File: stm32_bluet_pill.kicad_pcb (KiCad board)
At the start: 4 copper layers, 45.8 x 19.6 mm, 80 parts, among them J1 Conn_01x15, J2 Conn_01x15, J3 BAT_SOCKET, J4 Conn_ARM_SWD_TagConnect_TC203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, J5 USB_C_Plug_USB2.0, Q1 DMG1012T, U1 STM32WB55RGVx, U3 AT25SL321-U, U4 BQ25185, U5 TPS62746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

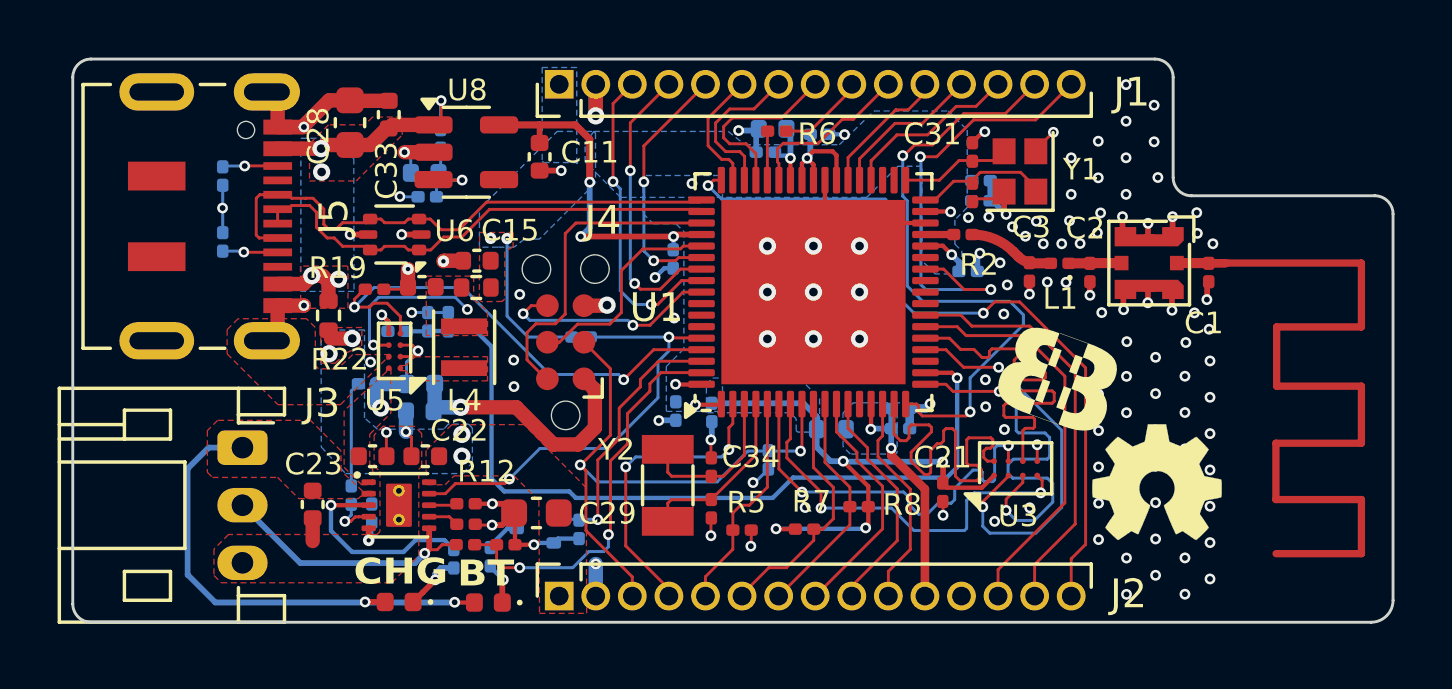
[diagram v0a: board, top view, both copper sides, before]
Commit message: Updated project
- Changed board stackup, trace-widths
- Changed VIA size
- Fixed fab drawings
- added CHG FLT LED
- Removed unnecessary files
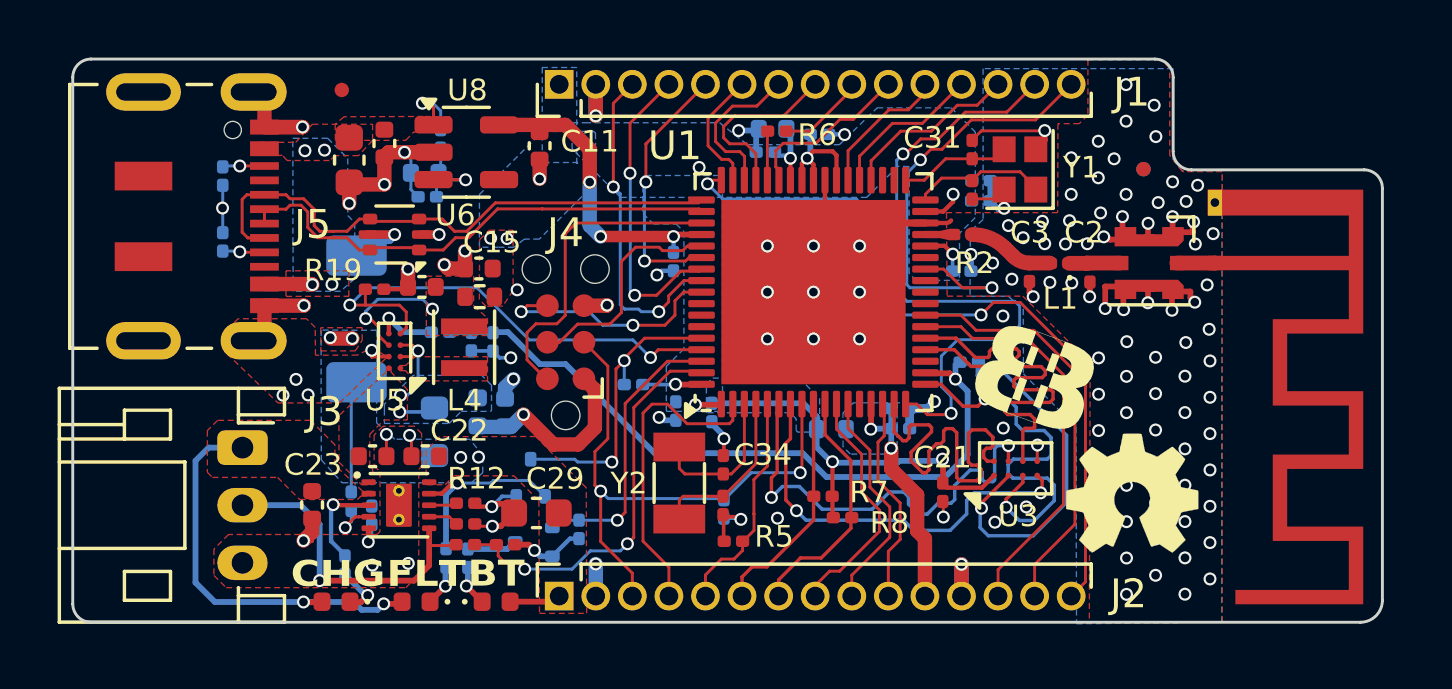
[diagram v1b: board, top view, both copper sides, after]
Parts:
- removed A1: 2.45GHz, user_antenna:nRF52_dongle_meander_F
- removed the REF** at (229.0, 143.7)
- added AE1: Antenna_Shield, RF_Antenna:Texas_SWRA117D_2.4GHz_Right, F.Cu at (231.1, 135.1)
- added D2: RB081LAM-20TR, Diode_SMD:D_SOD-128, B.Cu at (201.2, 137.0)
- added D5: LED, Diode_SMD:D_0402_1005Metric, F.Cu at (203.3, 146.9)
- added FID1: FID1, Fiducial:Fiducial_0.5mm_Mask1mm, F.Cu at (200.7, 129.1)
- added FID2: Fiducial, Fiducial:Fiducial_0.5mm_Mask1mm, F.Cu at (228.6, 131.8)
- added FID3: Fiducial, Fiducial:Fiducial_0.5mm_Mask1mm, B.Cu at (228.6, 131.8)
- added Q2: DMG1012T, Package_TO_SOT_SMD:SOT-523, B.Cu at (207.3, 142.6)
- added REF**: OSHW-Logo2_7.3x6mm_SilkScreen, Symbol:OSHW-Logo2_7.3x6mm_SilkScreen, F.Cu at (228.2, 143.8)
- C1: value 0.7PF -> 10NF; moved to B.Cu
- D3: value BAT54LP -> VSKY05301006-G4-08
- J4: value Conn_ARM_SWD_TagConnect_TC2030-NL -> J4
- R13: footprint Resistor_SMD:R_0201_0603Metric -> Resistor_SMD:R_0603_1608Metric
- R22: value 0R -> 420R; footprint Resistor_SMD:R_0402_1005Metric -> Resistor_SMD:R_0201_0603Metric; moved to B.Cu
- moved R22 9.36 mm to (204.3, 145.3)
- moved C1 8.88 mm to (222.5, 138.5), turned to 0 degrees
- moved R3 3.79 mm to (200.8, 145.6)
- moved C27 2.96 mm to (206.4, 140.3), turned to 90 degrees
- moved R13 2.86 mm to (203.9, 141.0), turned to -90 degrees
- moved R4 2.46 mm to (210.9, 139.3), turned to 180 degrees
- moved C10 2.30 mm to (214.0, 143.6)
- moved D3 2.20 mm to (205.4, 140.3), turned to -90 degrees
- moved D1 2.19 mm to (200.5, 146.9)
- moved C25 1.70 mm to (206.0, 137.8), turned to -90 degrees
- moved R17 1.66 mm to (205.2, 137.8), turned to -90 degrees
- moved R16 1.51 mm to (204.2, 137.5)
- moved R7 1.31 mm to (217.4, 143.2), turned to 180 degrees
- moved C28 1.30 mm to (201.0, 131.5), turned to -90 degrees
- moved C33 1.02 mm to (202.2, 130.9), turned to -90 degrees
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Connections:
- C1 pad 1: /BLE_MCU/BT_PCB_ANT -> VIN_SNS_ADC1_IN9
- D4 pad 2: PPVAR_BAT -> PPVAR_VIN
- R22 pad 1: VBUS -> FLT_CHG_ODL
- R22 pad 2: PPVAR_VIN -> Net-(D5-K)
- R4 pad 2: FLT_CHG_L -> /BLE_MCU/FLT_CHG_OD
- U1 pad 64: FLT_CHG_L -> /BLE_MCU/FLT_CHG_OD
- U4 pad 9: FLT_CHG_L -> FLT_CHG_ODL
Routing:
- net GND: track 66.6 -> 89.3 mm, vias 133 -> 137
- net FLT_CHG_L: track 15.5 -> 0.00 mm, vias 2 -> 0
- net /BLE_MCU/FLT_CHG_OD: track 0.00 -> 10.4 mm, vias 0 -> 2
- net PP1800_ALW: track 35.5 -> 27.4 mm, vias 12 -> 10
- net FLT_CHG_ODL: track 0.00 -> 6.89 mm, vias 0 -> 1
- net /POWER/CHG_LED_GRN: track 7.08 -> 3.14 mm
- net VIN_SNS_ADC1_IN9: track 28.9 -> 25.1 mm
- net VBUS: track 11.0 -> 7.59 mm
- net PPVAR_BAT: track 17.0 -> 14.4 mm
- net PP3300_DBG: track 9.25 -> 6.78 mm
- net /POWER/CHGR_BAT_THERM: track 9.31 -> 11.2 mm
- net PPVAR_VIN: track 4.39 -> 6.22 mm
- net /BLE_MCU/QSPI_MEM_D1: track 13.9 -> 15.7 mm
- net PP3300_VDDUSB: track 12.4 -> 10.9 mm
- net Net-(D5-K): track 0.00 -> 1.43 mm, vias 0 -> 1
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- added copper zone on B.Cu, net GND
- added copper zone on B.Cu, net PPVAR_SYS
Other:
- board size 45.8 x 19.6 mm -> 45.5 x 19.6 mm
- board text added: "0"
- board text added: "0 mm"
- board text added: "0.01 mm"
- board text added: "0.0152 mm"
- board text added: "0.02"
- board text added: "0.035 mm"
- board text added: "0.0764 mm"
- board text added: "0.1020 mm / 0.1000 mm"
- board text added: "0.2000 mm"
- board text added: "0.865 mm"
- board text added: "1"
- board text added: "1.1382 mm"
- board text added: "1080"
- board text added: "3.3"
- board text added: "3.91"
- board text added: "4"
- board text added: "4.6"
- board text added: "45.4770 mm x 19.5580 mm"
- board text added: "B.Cu"
- board text added: "B.Mask"
- board text added: "B.Paste"
- board text added: "B.Silkscreen"
- board text added: "BOARD CHARACTERISTICS"
- board text added: "Blue"
- board text added: "Board Thickness:"
- board text added: "Board overall dimensions:"
- board text added: "Bottom Silk Screen"
- board text added: "Bottom Solder Mask"
- board text added: "Bottom Solder Paste"
- board text added: "Castellated pads:"
- board text added: "Color"
- board text added: "Copper Finish:"
- board text added: "Copper Layer Count:"
- board text added: "Dielectric 1"
- board text added: "Dielectric 2"
- board text added: "Dielectric 3"
- board text added: "Edge card connectors:"
- board text added: "Epsilon R"
- board text added: "F.Cu"
- board text added: "F.Mask"
- board text added: "F.Paste"
- board text added: "F.Silkscreen"
- board text added: "FLT"
- board text added: "FR4"
- board text added: "FR4 natural"
- board text added: "IMPEDANCE TABLE"
- board text added: "Impedance Control:"
- board text added: "In1.Cu"
- board text added: "In2.Cu"
- board text added: "Layer Name"
- board text added: "Loss Tangent"
- board text added: "Material"
- board text added: "Min hole diameter:"
- board text added: "Min track/spacing:"
- board text added: "No"
- board text added: "No Copper Theiving in enclosed RF Areas"
- board text added: "None"
- board text added: "Not specified"
- board text added: "Plated Board Edge:"
- board text added: "Stackup (JLC04121H-1080)"
- board text added: "Thickness (mm)"
- board text added: "Top Silk Screen"
- board text added: "Top Solder Mask"
- board text added: "Top Solder Paste"
- board text added: "Type"
- board text added: "White"
- board text added: "Yes"
- board text added: "copper"
- board text added: "core"
- board text added: "prepreg"

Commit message: Various BOM and Bug Fixes * Changed Stackup to common JLCPCB stackup * Modified trace widths as per new stackup * Reduced drill hole size * Rotated uFL connector as per datasheet pinout * Added pop options for ADC voltage * removed some GPIO and added GND to headers * BOM changes for battery charger, USB connector etc. to support component specifications and USB standards. * Improved MCU bypass and power delivery routing * Various other small bug fixes
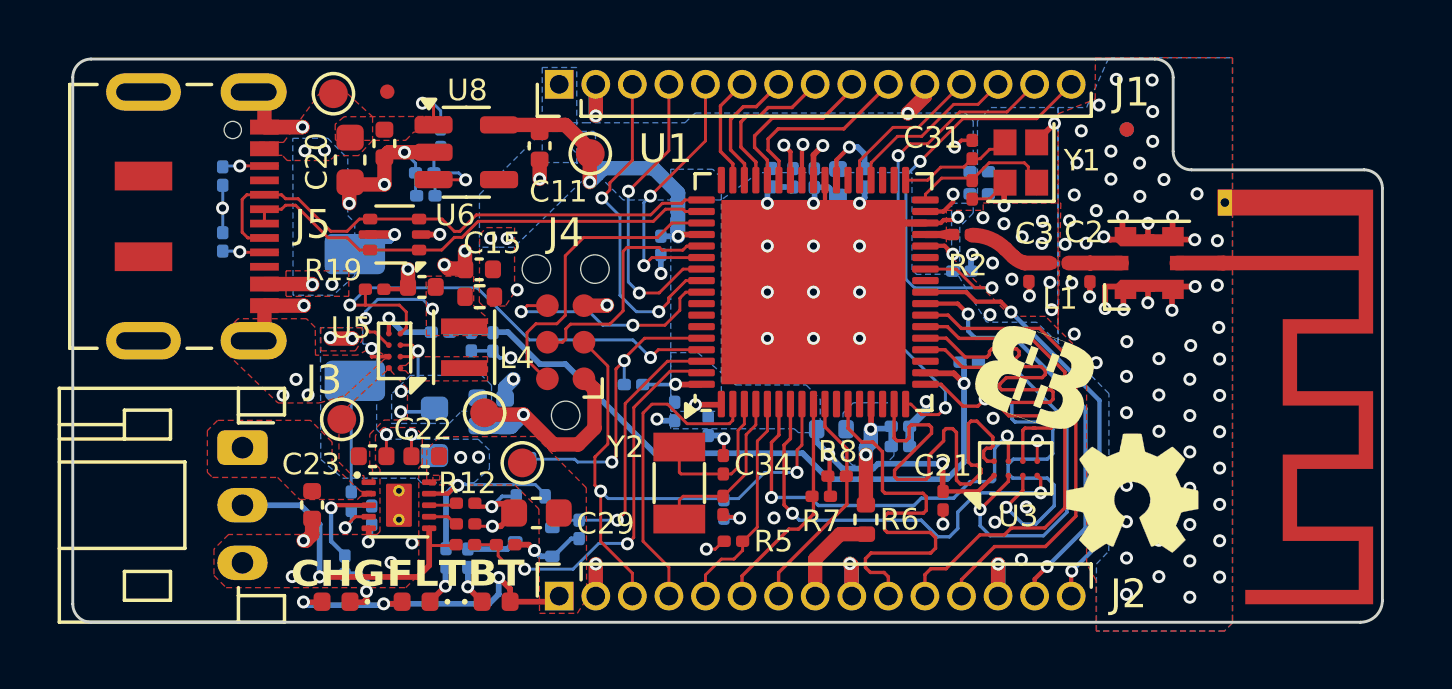
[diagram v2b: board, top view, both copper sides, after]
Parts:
- added C19: 100N, Capacitor_SMD:C_0201_0603Metric, B.Cu at (216.4, 132.1)
- added C20: 2.2U 35V, Capacitor_SMD:C_0603_1608Metric, F.Cu at (201.0, 131.5)
- added TP4: TestPoint, TestPoint:TestPoint_Pad_D1.0mm, F.Cu at (200.7, 140.5)
- added TP5: TestPoint, TestPoint:TestPoint_Pad_D1.0mm, F.Cu at (207.0, 142.0)
- added TP6: TestPoint, TestPoint:TestPoint_Pad_D1.0mm, F.Cu at (205.7, 140.3)
- added TP7: TestPoint, TestPoint:TestPoint_Pad_D1.0mm, F.Cu at (200.4, 129.2)
- added TP8: TestPoint, TestPoint:TestPoint_Pad_D1.0mm, F.Cu at (209.4, 131.3)
- AE1: value Antenna_Shield -> PCB MIFA
- C1: value 10NF -> 10N
- C10, C13, C17, C21, C25, C4, C5, C6, C7, C8, C9: value 100NF -> 100N
- C11, C12, C15: value 4.7UF -> 4.7U
- C14: value 100PF -> 100P
- C16: value 1UF -> 1.0U
- C2, C3: value 0.7PF -> 0.7P
- C22, C33: value 1.0UF -> 1.0U
- C23, C29: value 4.7UF -> 1.0U 35V
- C24: value 4.7UF -> 10U 10V
- C26: value 10UF -> 10U
- C27: value 1.0UF -> 1.0U 16V
- C28: value 4.7UF -> 100N; footprint Capacitor_SMD:C_0603_1608Metric -> Capacitor_SMD:C_0201_0603Metric; moved to B.Cu
- C30: footprint Capacitor_SMD:C_0402_1005Metric -> Capacitor_SMD:C_0201_0603Metric
- FID1: value FID1 -> Fiducial
- J3: value BAT_SOCKET -> PH_S3B-PH-K
- J4: value J4 -> Conn_ARM_SWD_TagConnect_TC2030-NL
- J5: value USB_C_Plug_USB2.0 -> DX07S016JA1R1500
- L1: value 2.2NH -> 2.2N
- L4: value 2.2UH -> 2.2U
- R22, R3: value 420R -> 470R
- R24: value 420R -> 1K
- R6: value 22R -> 0R; footprint Resistor_SMD:R_0201_0603Metric -> Resistor_SMD:R_0402_1005Metric
- Y1: value 32MHz -> ECS-320-8-37CKM
- Y2: value 32.768k -> SC32S-7PF20PPM
- moved C28 14.7 mm to (215.7, 132.1)
- moved R6 13.8 mm to (218.9, 144.0), turned to -90 degrees
- moved C6 3.56 mm to (218.9, 132.1), turned to -90 degrees
- moved C12 2.94 mm to (218.0, 132.3), turned to -90 degrees
- moved FID1 1.58 mm to (202.3, 129.2)
- moved C7 1.53 mm to (217.1, 132.2), turned to -90 degrees
- moved FID2 1.50 mm to (228.0, 130.5)
- moved FID3 1.50 mm to (228.0, 130.5)
- moved R8 1.45 mm to (217.9, 142.5)
- moved C9 0.71 mm to (211.8, 134.5)
- moved C16 0.62 mm to (220.1, 141.5)
- moved C17 0.62 mm to (220.1, 140.8)
- moved C4 0.50 mm to (213.5, 140.8)
- moved AE1 0.34 mm to (231.4, 135.1)
- moved C13 0.32 mm to (222.9, 131.9)
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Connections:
- C28 pad 1: VBUS -> PP1800_ALW
- D1 pad 2: PPVAR_BAT -> PPVAR_VIN
- D5 pad 2: PPVAR_BAT -> PPVAR_VIN
- J1 pad 11: GPIO_PE4 -> GND
- J2 pad 10: ADC1_IN5 -> STM_SAI1_SD_A
- J2 pad 11: PPVAR_ADC -> STM_SAI1_SCK_A
- J2 pad 12: GND -> STM_SAI1_FS_A
- J2 pad 13: STM_SAI1_SCK_A -> GND
- J2 pad 14: STM_SAI1_FS_A -> ADC1_IN13
- J2 pad 15: STM_SAI1_SD_A -> ADC1_IN14
- J2 pad 8: ADC1_IN3 -> Net-(J2-Pin_8)
- J2 pad 9: ADC1_IN4 -> GND
- R6 pad 1: Net-(U1-PB13) -> PPVAR_ADC
- R6 pad 2: SPI2_CLK_PB13 -> Net-(J2-Pin_8)
- TP1 pad A: /BLE_MCU/BT_ANT_UFL -> /BLE_MCU/BT_PCB_ANT
- TP1 pad C: /BLE_MCU/BT_PCB_ANT -> /BLE_MCU/BT_ANT_UFL
- U1 pad 11: ADC1_IN3 -> unconnected-(U1-PC2-Pad11)
- U1 pad 12: ADC1_IN4 -> STM_SAI1_SD_A
- U1 pad 15: ADC1_IN5 -> unconnected-(U1-PA0-Pad15)
- U1 pad 25: unconnected-(U1-PC4-Pad25) -> ADC1_IN13
- U1 pad 26: unconnected-(U1-PC5-Pad26) -> ADC1_IN14
- U1 pad 40: GPIO_PE4 -> unconnected-(U1-PE4-Pad40)
- U1 pad 47: Net-(U1-PB13) -> SPI2_CLK_PB13
- U1 pad 51: STM_SAI1_SD_A -> unconnected-(U1-PA10-Pad51)
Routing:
- net ADC1_IN14: track 0.00 -> 14.8 mm, vias 0 -> 2
- net ADC1_IN13: track 0.00 -> 14.7 mm, vias 0 -> 2
- net PPVAR_BAT: track 14.4 -> 0.00 mm, vias 2 -> 0
- net STM_SAI1_SD_A: track 26.2 -> 14.5 mm, vias 2 -> 0
- net PPVAR_VIN: track 6.22 -> 16.1 mm, vias 4 -> 7
- net ADC1_IN3: track 8.41 -> 0.00 mm
- net ADC1_IN4: track 7.81 -> 0.00 mm
- net ADC1_IN5: track 7.27 -> 0.00 mm
- net PP1800_ALW: track 27.4 -> 21.3 mm, vias 10 -> 12
- net STM_LPUART_TXD_PA2: track 22.6 -> 16.8 mm
- net GPIO_PE4: track 4.84 -> 0.00 mm
- net Net-(J2-Pin_8): track 0.00 -> 3.77 mm
- net PPVAR_ADC: track 8.59 -> 4.97 mm
- net SPI2_CLK_PB13: track 3.06 -> 5.94 mm
- net STM_SAI1_SCK_A: track 14.2 -> 16.8 mm
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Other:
- board text added: "0.2500 mm"
- board text added: "0.7 mm"
- board text added: "0.9732 mm"
- board text added: "3V3"
- board text added: "45.48 mm x 19.56 mm"
- board text added: "GND"
- board text added: "RST"
- board text added: "SCK"
- board text added: "STM32 BLUET PILL Ver. 2"
- board text added: "SWD"
- board text added: "SWO"
- board text added: "Stackup (JLC04101H-1080)"
- board text removed: "0.2000 mm"
- board text removed: "0.865 mm"
- board text removed: "1.1382 mm"
- board text removed: "45.4770 mm x 19.5580 mm"
- board text removed: "Stackup (JLC04121H-1080)"
